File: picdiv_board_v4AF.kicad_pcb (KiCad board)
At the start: 2 copper layers, 100 x 99.5 mm, 77 parts, among them J1 DC-Input, J10 PPS_B, J11 PPS_B, J2 MountingHole_M2.5, J3 MountingHole_M2.5, J4 TEST_1PPS, J5 Conn_01x06, J6 Sync, J7 Sync, J8 10MHz, J9 10MHz, SW1 SW_DIP_x03, U1 LT1963AEST-3.3, U2 LT1963AEST-3.3, U3 PIC12F675-xSN, U4 LTC6993xS6-1, U5 IDT5PB1108, U6 IDT5PB1108, U7 LT1963AEQ, U8 ADR4540

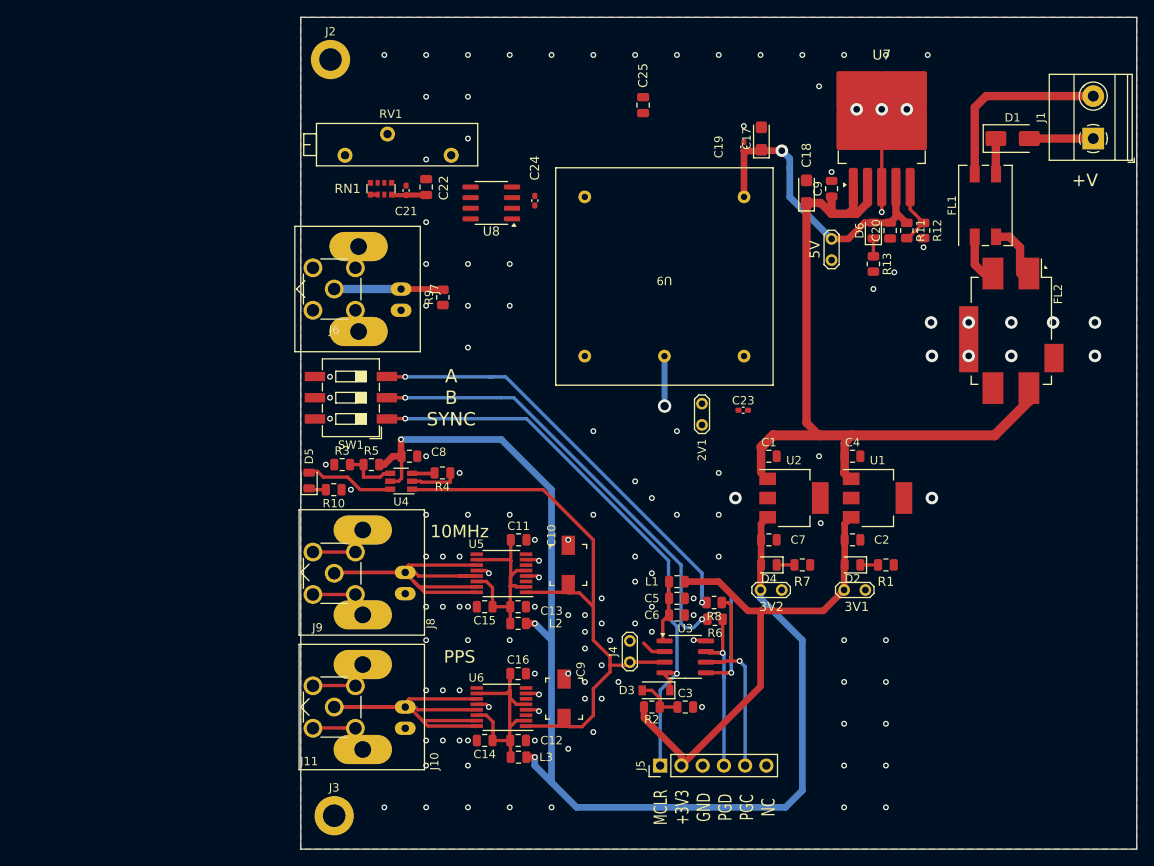
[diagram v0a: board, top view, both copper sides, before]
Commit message: More layout
Vadj getting closer.   Keep out around OCXO
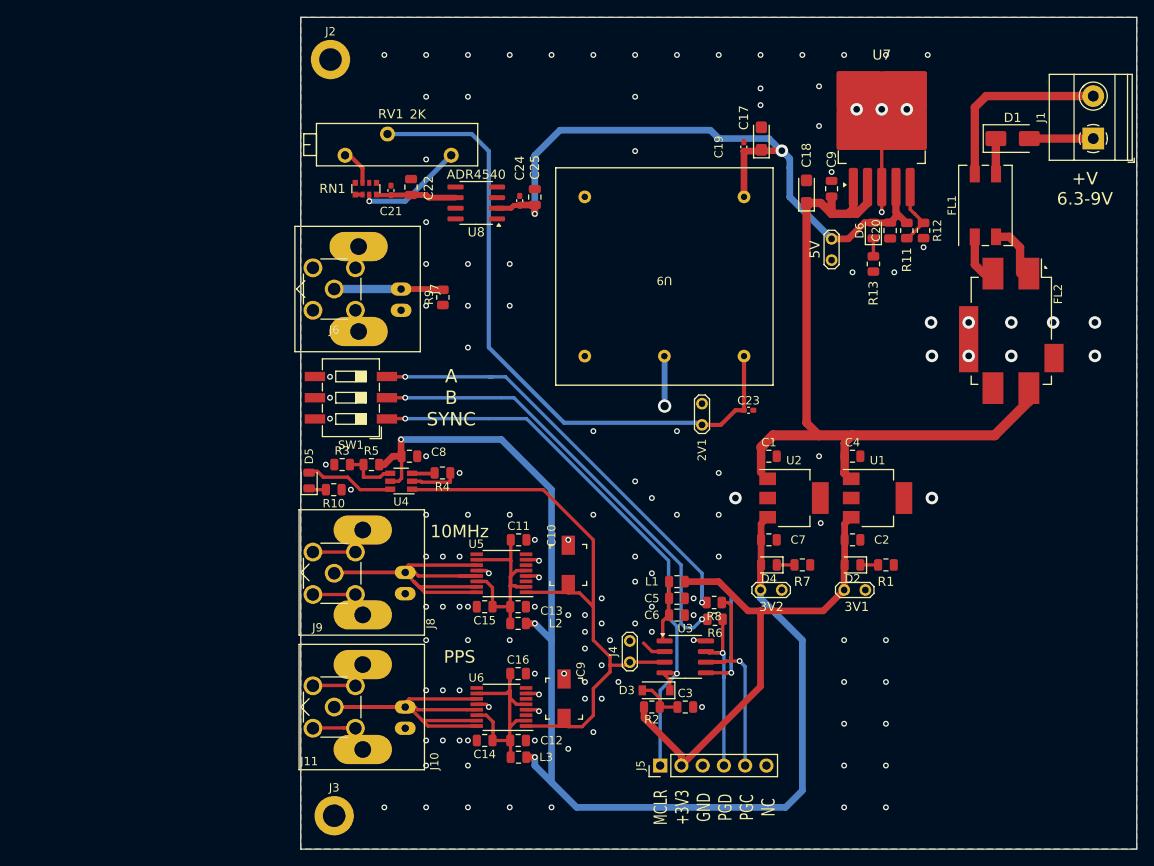
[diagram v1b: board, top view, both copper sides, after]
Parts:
- moved C25 17.0 mm to (153.0, 72.0)
- moved C21 1.81 mm to (135.8, 71.2)
- moved C22 1.81 mm to (138.2, 70.8)
- moved C24 1.81 mm to (151.2, 72.4)
- moved RN1 1.81 mm to (132.8, 71.0)
- moved U8 1.81 mm to (146.0, 72.7)
- moved C23 0.63 mm to (178.6, 97.5)
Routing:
- net Vadj: track 0.00 -> 78.0 mm
- net +5V: track 40.3 -> 84.9 mm, vias 1 -> 2
- net Net-(RN1-R2.2): track 0.00 -> 12.9 mm, vias 0 -> 1
- net Net-(RN1-R1.2): track 4.17 -> 9.62 mm
- net Net-(RN1-R3.1): track 0.00 -> 4.49 mm
- net GND: vias 139 -> 142
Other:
- board text added: "+V 6.3-9V"
- board text removed: "+V"

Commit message: Hmmm
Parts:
- moved C10 16.0 mm to (156.5, 132.0)
- moved C9 16.0 mm to (157.0, 116.0)
- moved J4 0.87 mm to (163.5, 127.6)
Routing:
- net PPS: track 70.4 -> 37.3 mm
- net 10MHz: track 2.72 -> 20.1 mm
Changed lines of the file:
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@@
 	(footprint "TestPoint:TestPoint_2Pads_Pitch2.54mm_Drill0.8mm"
 		(layer "F.Cu")
-		(at 164.365 127.635 90)
+		(at 163.5 127.635 90)
 		(descr "Test point with 2 pins, pitch 2.54mm, drill diameter 0.8mm")
 		(tags "CONN DEV")
@@
 	(footprint "Capacitor_SMD:C_Trimmer_Murata_TZB4-A"
 		(layer "F.Cu")
-		(at 156.5 132 -90)
+		(at 157 116 -90)
 		(descr "trimmer capacitor SMD horizontal, http://www.murata.com/~/media/webrenewal/support/library/catalog/products/capacitor/trimmer/t13e.ashx?la=en-gb")
 		(tags " Murata TZB4 TZB4-A")
@@
 		)
 		(property "Footprint" "Capacitor_SMD:C_Trimmer_Murata_TZB4-A"
-			(at 0 0 -90)
+			(at 0 0 90)
 			(layer "F.Fab")
 			(hide yes)
@@
 		)
 		(property "Datasheet" ""
-			(at 0 0 -90)
+			(at 0 0 90)
 			(layer "F.Fab")
 			(hide yes)
@@
 		)
 		(property "Description" "Trimmable capacitor"
-			(at 0 0 -90)
+			(at 0 0 90)
 			(layer "F.Fab")
 			(hide yes)
@@
 	(footprint "Capacitor_SMD:C_Trimmer_Murata_TZB4-A"
 		(layer "F.Cu")
-		(at 157 116 90)
+		(at 156.5 132 90)
 		(descr "trimmer capacitor SMD horizontal, http://www.murata.com/~/media/webrenewal/support/library/catalog/products/capacitor/trimmer/t13e.ashx?la=en-gb")
 		(tags " Murata TZB4 TZB4-A")
@@
 	)
 	(via
-		(at 161 120)
+		(at 161 118)
 		(size 0.7)
 		(drill 0.4)
@@
 	)
 	(via
-		(at 165 123)
+		(at 165 121)
 		(size 0.7)
 		(drill 0.4)
@@
 	)
 	(segment
-		(start 160 125)
-		(end 160 121)
-		(width 0.4)
-		(layer "F.Cu")
-		(net 3)
-	)
-	(segment
-		(start 151.95 119.275)
-		(end 156.925 119.275)
-		(width 0.4)
-		(layer "F.Cu")
-		(net 3)
-	)
-	(segment
-		(start 162 128)
-		(end 162 127)
-		(width 0.4)
-		(layer "F.Cu")
-		(net 3)
-	)
-	(segment
 		(start 154 107)
 		(end 138.62 107)
@@
 	)
 	(segment
-		(start 160 121)
-		(end 160 113)
-		(width 0.4)
-		(layer "F.Cu")
-		(net 3)
-	)
-	(segment
 		(start 168.3 127.635)
 		(end 164.365 127.635)
@@
 	)
 	(segment
-		(start 162 127)
-		(end 160 125)
-		(width 0.4)
-		(layer "F.Cu")
-		(net 3)
-	)
-	(segment
-		(start 160 113)
-		(end 154 107)
-		(width 0.4)
-		(layer "F.Cu")
-		(net 3)
-	)
-	(segment
-		(start 160 121)
-		(end 158.35 119.35)
-		(width 0.4)
-		(layer "F.Cu")
-		(net 3)
-	)
-	(segment
 		(start 164 128)
 		(end 162 128)
@@
 	)
 	(segment
-		(start 158.35 119.35)
-		(end 157 119.35)
-		(width 0.4)
-		(layer "F.Cu")
-		(net 3)
-	)
-	(segment
-		(start 156.925 119.275)
-		(end 157 119.35)
-		(width 0.4)
-		(layer "F.Cu")
-		(net 3)
-	)
-	(segment
 		(start 178.025 91.025)
 		(end 178.025 97.475)
@@
 	)
 	(segment
+		(start 156.075 119.275)
+		(end 157 118.35)
+		(width 0.4)
+		(layer "F.Cu")
+		(net 45)
+	)
+	(segment
+		(start 151.95 119.275)
+		(end 156.075 119.275)
+		(width 0.4)
+		(layer "F.Cu")
+		(net 45)
+	)
+	(segment
+		(start 159.01 118.35)
+		(end 157 118.35)
+		(width 0.4)
+		(layer "F.Cu")
+		(net 45)
+	)
+	(segment
 		(start 168.3 126.365)
 		(end 167.025 126.365)
@@
 	(segment
 		(start 167.025 126.365)
-		(end 166 125.34)
+		(end 159.01 118.35)
 		(width 0.4)
 		(layer "F.Cu")

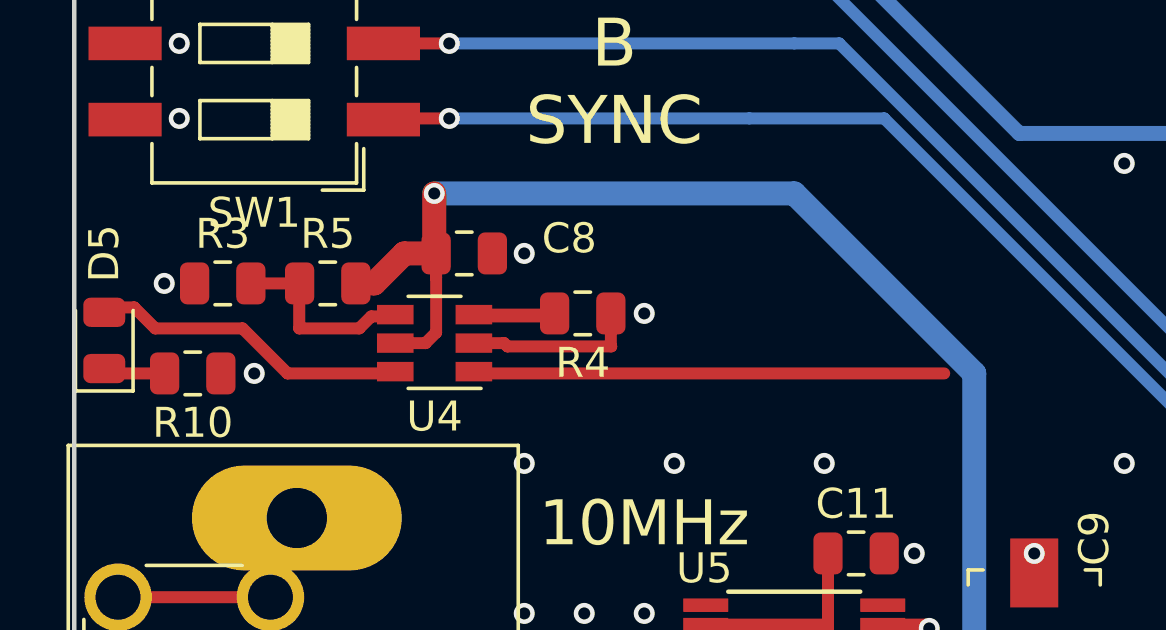
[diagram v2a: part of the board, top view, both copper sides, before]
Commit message: Led Blink
Replace pricey LT monostable with an NE555.  No need for an expensive part.
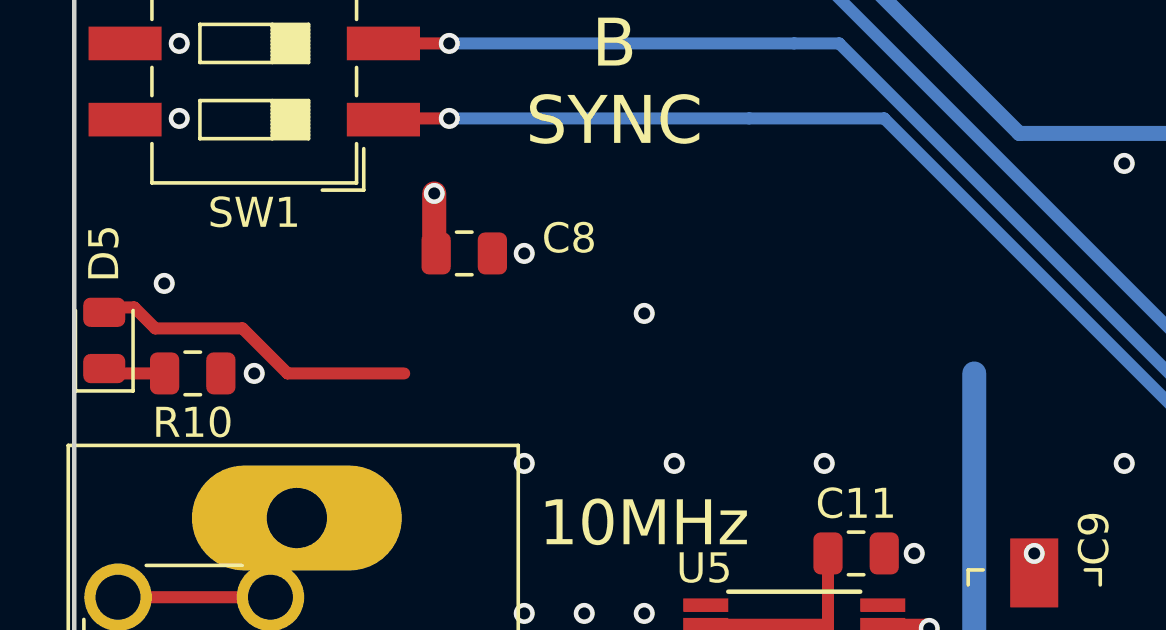
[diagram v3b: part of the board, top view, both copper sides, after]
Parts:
- removed R3: 523k, Resistor_SMD:R_0805_2012Metric
- removed R4: 300k, Resistor_SMD:R_0805_2012Metric
- removed R5: 1M, Resistor_SMD:R_0805_2012Metric
- removed U4: LTC6993xS6-1, Package_TO_SOT_SMD:TSOT-23-6
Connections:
- D5 pad 2: Net-(D5-A) -> unconnected-(D5-A-Pad2)
- J4 pad 1: PPS -> unconnected-(J4-Pad1)
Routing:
- net 3V3_OUT: track 140.7 -> 113.0 mm
- net PPS: track 37.3 -> 21.9 mm
- net unconnected-(D5-A-Pad2): track 0.00 -> 10.9 mm
- net Net-(D5-A): track 10.9 -> 0.00 mm
- net Net-(U4-DIV): track 6.77 -> 0.00 mm
- net GND: track 61.3 -> 55.6 mm
- net Net-(U4-SET): track 5.13 -> 0.00 mm

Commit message: 555 work
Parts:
- added C26: 100n, Capacitor_SMD:C_0805_2012Metric, F.Cu at (106.6, 64.3)
- added C27: 100n, Capacitor_SMD:C_0805_2012Metric, F.Cu at (106.6, 67.3)
- added C28: 100n, Capacitor_SMD:C_0805_2012Metric, F.Cu at (106.6, 70.3)
- added L4: 2u2, Inductor_SMD:L_0805_2012Metric, F.Cu at (111.1, 67.7)
- added R3: R, Resistor_SMD:R_0805_2012Metric, F.Cu at (149.0, 107.0)
- added U4: NE555D, Package_SO:SOIC-8_3.9x4.9mm_P1.27mm, F.Cu at (138.0, 105.0)
- C8: value 100nF -> C
- moved C8 10.0 mm to (148.0, 104.0)
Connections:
- C8 pad 1: 3V3_OUT -> Net-(U4-DIS)
- D5 pad 2: unconnected-(D5-A-Pad2) -> Net-(D5-A)
- J4 pad 1: unconnected-(J4-Pad1) -> PPS
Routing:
- net 3V3_OUT: track 113.0 -> 92.9 mm, vias 3 -> 2
- net unconnected-(D5-A-Pad2): track 10.9 -> 0.00 mm
- net Net-(D5-A): track 0.00 -> 9.80 mm
- net GND: vias 142 -> 140

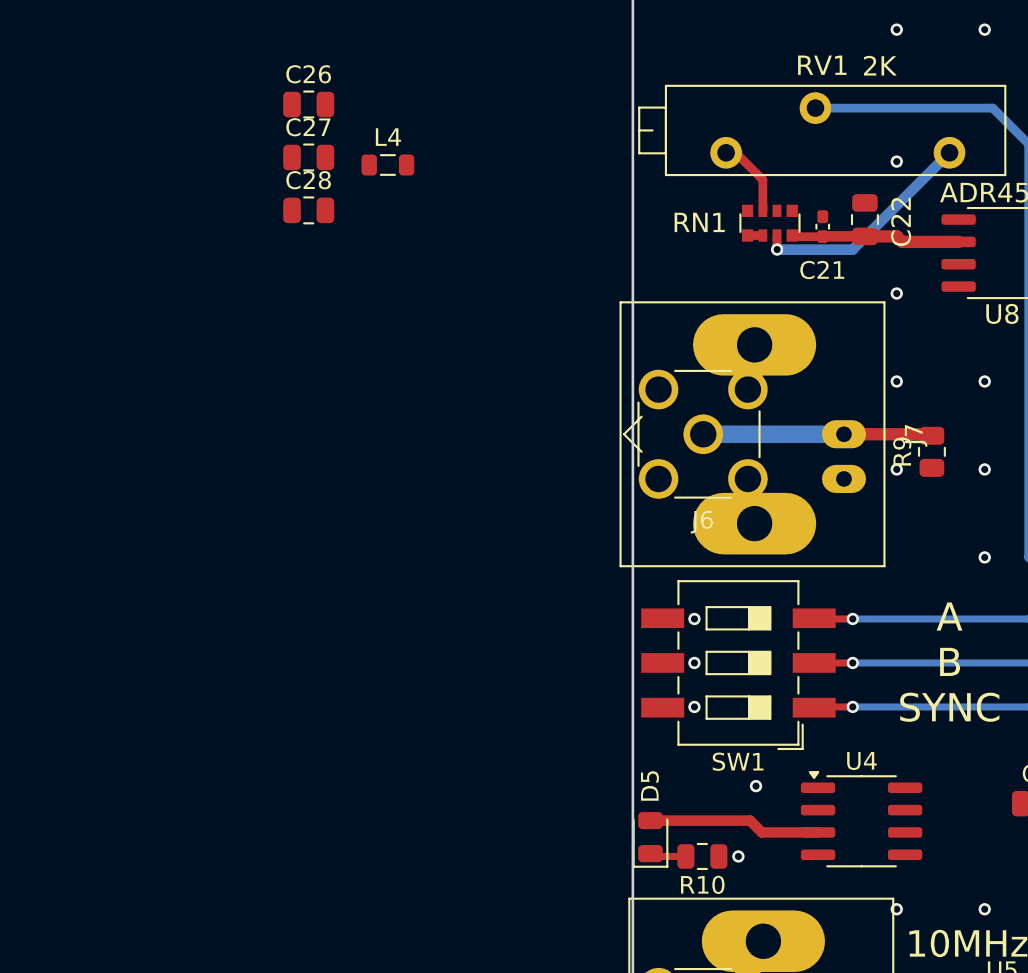
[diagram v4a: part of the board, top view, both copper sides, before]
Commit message: Add inverter to 555 input.
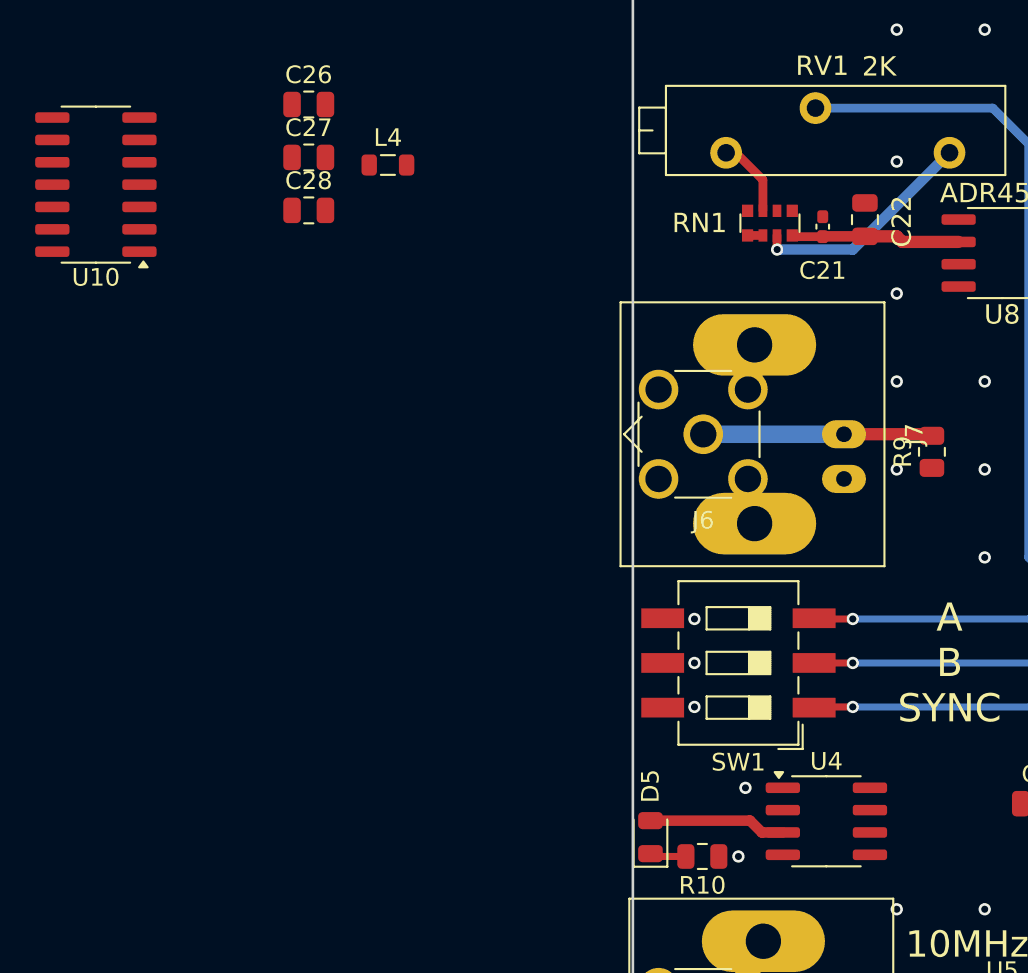
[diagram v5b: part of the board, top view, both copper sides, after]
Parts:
- added U10: 74HC14, Package_SO:SOIC-14_3.9x8.7mm_P1.27mm, F.Cu at (94.5, 68.8)
- C8: value C -> 1µF
- moved U4 2.00 mm to (136.0, 105.0)
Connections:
- J4 pad 1: PPS -> Net-(U4-TR)
- U4 pad 2: PPS -> Net-(U4-TR)
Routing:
- net Net-(D5-A): track 9.80 -> 7.80 mm

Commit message: 555 stuff
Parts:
- C3: value C -> 100n
- R3: value R -> 1.8K
- moved U10 68.4 mm to (152.5, 105.0), turned to 0 degrees
- moved C26 52.6 mm to (143.2, 102.0), turned to 90 degrees
- moved C28 52.6 mm to (145.5, 105.6), turned to 90 degrees
- moved C27 48.9 mm to (141.0, 102.0), turned to 90 degrees
- moved L4 48.4 mm to (145.3, 101.9), turned to -90 degrees
- moved R3 8.12 mm to (141.0, 105.6), turned to -90 degrees
- moved C8 4.96 mm to (143.3, 105.6), turned to 90 degrees
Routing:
- net GND: vias 140 -> 139

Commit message: 555
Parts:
- added C29: 100n, Capacitor_SMD:C_0805_2012Metric, F.Cu at (160.0, 101.0)
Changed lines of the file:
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@@
 		(tags "SOIC SO")
 		(property "Reference" "U10"
-			(at 0 -5.28 360)
+			(at 0 -5.28 0)
 			(layer "F.SilkS")
 			(effects
@@
 		)
 		(property "Value" "74HC14"
-			(at 0 5.28 360)
+			(at 0 5.28 0)
 			(layer "F.Fab")
 			(effects
@@
 		)
 		(fp_text user "${REFERENCE}"
-			(at 0 0 360)
+			(at 0 0 0)
 			(layer "F.Fab")
 			(effects
@@
 			(offset
 				(xyz 0 0 0)
+			)
+			(scale
+				(xyz 1 1 1)
+			)
+			(rotate
+				(xyz 0 0 0)
+			)
+		)
+	)
+	(footprint "Capacitor_SMD:C_0805_2012Metric"
+		(layer "F.Cu")
+		(at 160 101)
+		(descr "Capacitor SMD 0805 (2012 Metric), square (rectangular) end terminal, IPC_7351 nominal, (Body size source: IPC-SM-782 page 76, https://www.pcb-3d.com/wordpress/wp-content/uploads/ipc-sm-782a_amendment_1_and_2.pdf, https://docs.google.com/spreadsheets/d/1BsfQQcO9C6DZCsRaXUlFlo91Tg2WpOkGARC1WS5S8t0/edit?usp=sharing), generated with kicad-footprint-generator")
+		(tags "capacitor")
+		(property "Reference" "C29"
+			(at 0 -1.68 0)
+			(layer "F.SilkS")
+			(effects
+				(font
+					(size 1 1)
+					(thickness 0.15)
+				)
+			)
+		)
+		(property "Value" "100n"
+			(at 0 1.68 0)
+			(layer "F.Fab")
+			(effects
+				(font
+					(size 1 1)
+					(thickness 0.15)
+				)
+			)
+		)
+		(property "Footprint" "Capacitor_SMD:C_0805_2012Metric"
+			(at 0 0 0)
+			(unlocked yes)
+			(layer "F.Fab")
+			(hide yes)
+			(effects
+				(font
+					(size 1.27 1.27)
+					(thickness 0.15)
+				)
+			)
+		)
+		(property "Datasheet" ""
+			(at 0 0 0)
+			(unlocked yes)
+			(layer "F.Fab")
+			(hide yes)
+			(effects
+				(font
+					(size 1.27 1.27)
+					(thickness 0.15)
+				)
+			)
+		)
+		(property "Description" "Unpolarized capacitor"
+			(at 0 0 0)
+			(unlocked yes)
+			(layer "F.Fab")
+			(hide yes)
+			(effects
+				(font
+					(size 1.27 1.27)
+					(thickness 0.15)
+				)
+			)
+		)
+		(property "MPN" "CC0805KRX7R9BB104"
+			(at 0 0 0)
+			(unlocked yes)
+			(layer "F.Fab")
+			(hide yes)
+			(effects
+				(font
+					(size 1 1)
+					(thickness 0.15)
+				)
+			)
+		)
+		(property "LCSC" "C49678"
+			(at 0 0 0)
+			(unlocked yes)
+			(layer "F.Fab")
+			(hide yes)
+			(effects
+				(font
+					(size 1 1)
+					(thickness 0.15)
+				)
+			)
+		)
+		(property ki_fp_filters "C_*")
+		(sheetname "Root")
+		(sheetfile "picdiv_board_v4AF.kicad_sch")
+		(attr smd)
+		(fp_line
+			(start -0.261252 -0.735)
+			(end 0.261252 -0.735)
+			(stroke
+				(width 0.12)
+				(type solid)
+			)
+			(layer "F.SilkS")
+		)
+		(fp_line
+			(start -0.261252 0.735)
+			(end 0.261252 0.735)
+			(stroke
+				(width 0.12)
+				(type solid)
+			)
+			(layer "F.SilkS")
+		)
+		(fp_line
+			(start -1.7 -0.98)
+			(end 1.7 -0.98)
+			(stroke
+				(width 0.05)
+				(type solid)
+			)
+			(layer "F.CrtYd")
+		)
+		(fp_line
+			(start -1.7 0.98)
+			(end -1.7 -0.98)
+			(stroke
+				(width 0.05)
+				(type solid)
+			)
+			(layer "F.CrtYd")
+		)
+		(fp_line
+			(start 1.7 -0.98)
+			(end 1.7 0.98)
+			(stroke
+				(width 0.05)
+				(type solid)
+			)
+			(layer "F.CrtYd")
+		)
+		(fp_line
+			(start 1.7 0.98)
+			(end -1.7 0.98)
+			(stroke
+				(width 0.05)
+				(type solid)
+			)
+			(layer "F.CrtYd")
+		)
+		(fp_line
+			(start -1 -0.625)
+			(end 1 -0.625)
+			(stroke
+				(width 0.1)
+				(type solid)
+			)
+			(layer "F.Fab")
+		)
+		(fp_line
+			(start -1 0.625)
+			(end -1 -0.625)
+			(stroke
+				(width 0.1)
+				(type solid)
+			)
+			(layer "F.Fab")
+		)
+		(fp_line
+			(start 1 -0.625)
+			(end 1 0.625)
+			(stroke
+				(width 0.1)
+				(type solid)
+			)
+			(layer "F.Fab")
+		)
+		(fp_line
+			(start 1 0.625)
+			(end -1 0.625)
+			(stroke
+				(width 0.1)
+				(type solid)
+			)
+			(layer "F.Fab")
+		)
+		(fp_text user "${REFERENCE}"
+			(at 0 0 0)
+			(layer "F.Fab")
+			(effects
+				(font
+					(size 0.5 0.5)
+					(thickness 0.08)
+				)
+			)
+		)
+		(pad "1" smd roundrect
+			(at -0.95 0)
+			(size 1 1.45)
+			(layers "F.Cu" "F.Paste" "F.Mask")
+			(roundrect_rratio 0.25)
+			(net 16 "3V3_PIC")
+			(pintype "passive")
+		)
+		(pad "2" smd roundrect
+			(at 0.95 0)
+			(size 1 1.45)
+			(layers "F.Cu" "F.Paste" "F.Mask")
+			(roundrect_rratio 0.25)
+			(net 2 "GND")
+			(pintype "passive")
+		)
+		(model "${KICAD8_3DMODEL_DIR}/Capacitor_SMD.3dshapes/C_0805_2012Metric.wrl"
+			(offset
+				(xyz 0 0 0)
